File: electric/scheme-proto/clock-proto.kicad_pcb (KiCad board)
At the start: 2 copper layers, 60.5 x 88.5 mm, 134 parts, among them K1 servo, K2 1-wire, P1 batt, P10 led, P11 p2, P12 btn-4, P13 led, P14 led, P15 btn-5, P2 speaker, P3 dist, P4 btn-1, P5 btn-2, P6 btn-3, P7 led, P8 p1, P9 p3, Q1 bc857, Q10 bc847, Q11 bc847, Q12 bc857, Q13 bc857, Q14 bc847, Q15 bc847, Q16 bc847, Q17 bc857, Q18 bc857, Q2 bc847, Q3 bc857, Q4 bc847, Q5 irlml2244, Q6 bc847, Q7 bc857, Q8 bc847, Q9 bc857, U1 3310-LCD, U2 AD8607_2, U3 SD, U4 MINI-USB-B, U5 AD8607_2, U6 NCP3063, U7 NCP3063, U8 DS18S20

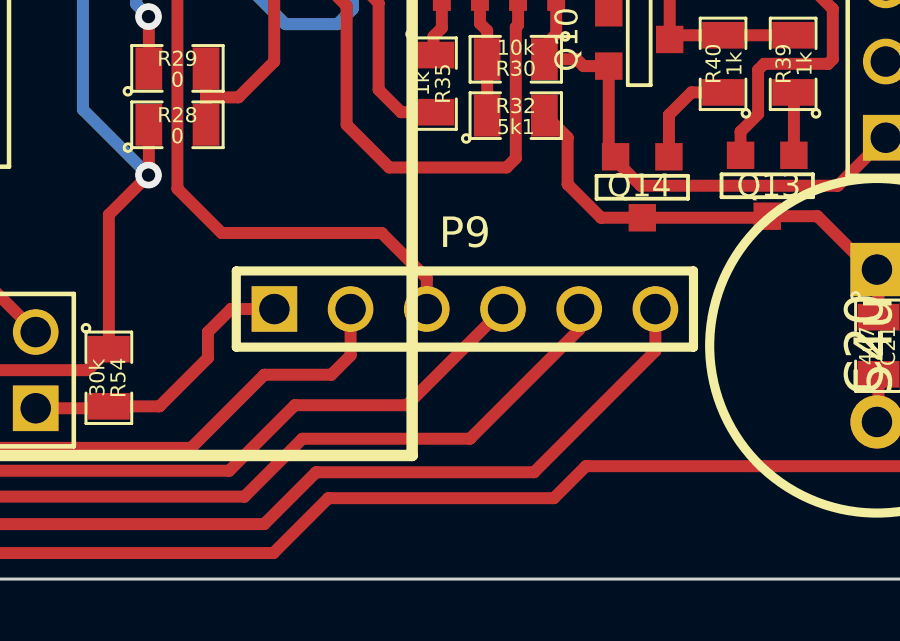
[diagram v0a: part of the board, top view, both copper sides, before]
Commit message: Shifted horizontal socket a bit upwards because, it didn't match the one on Disccovery board.
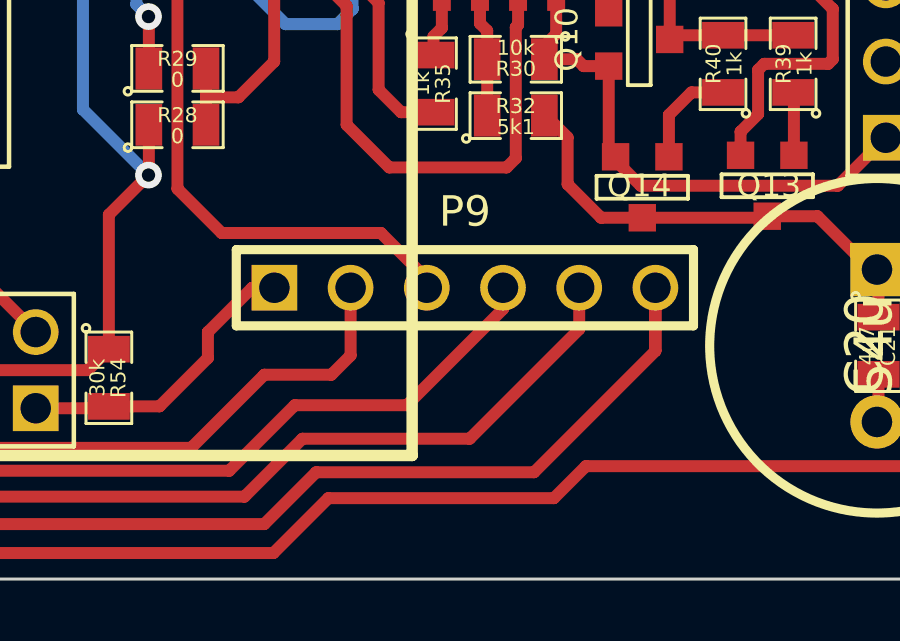
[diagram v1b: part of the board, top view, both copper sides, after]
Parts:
- moved P9 0.71 mm to (150.4, 139.3)
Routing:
- net /pb15: track 62.2 -> 65.0 mm
- net /pb12: track 35.6 -> 34.9 mm
- net /pb13: track 38.4 -> 39.1 mm
- net /btn-5: track 19.3 -> 20.0 mm
- net /pb14: track 37.4 -> 38.1 mm
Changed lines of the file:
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@@
     (area 119.449999 58.01106 180.050001 149.050001)
     (thickness 1.6)
-    (drawings 9)
-    (tracks 1178)
+    (drawings 10)
+    (tracks 1181)
     (zones 0)
     (modules 134)
@@
   )
   (setup
-    (last_trace_width 0.254)
+    (last_trace_width 0.4)
     (user_trace_width 0.4)
     (user_trace_width 0.6)
@@
   )
   (module PIN_ARRAY_6x1 (layer F.Cu)
-    (at 150.45 140)
+    (at 150.45 139.29)
     (descr "Double rangee de contacts 2 x 5 pins")
     (tags CONN)
@@
     )
   )
+  (gr_line (start 143.3 139.3) (end 157.4 139.3) (angle 90) (layer Dwgs.User) (width 0.2))
   (gr_line (start 119.5 149) (end 180 149) (angle 90) (layer Edge.Cuts) (width 0.1))
   (gr_line (start 124.5 60.5) (end 180 60.5) (angle 90) (layer Edge.Cuts) (width 0.1))
@@
   (segment (start 164.48 86.03) (end 164.6299 86.03) (width 0.4) (layer F.Cu) (net 12))
   (segment (start 164.6299 86.03) (end 168.5163 82.1436) (width 0.4) (layer F.Cu) (net 12))
+  (segment (start 141.8906 140.7606) (end 143.3612 139.29) (width 0.4) (layer F.Cu) (net 13) (status 800000))
+  (segment (start 143.3612 139.29) (end 144.1 139.29) (width 0.4) (layer F.Cu) (net 13) (status C00000))
   (segment (start 138.5824 143.2433) (end 140.2715 143.2433) (width 0.4) (layer F.Cu) (net 13))
-  (segment (start 142.6512 140) (end 144.1 140) (width 0.4) (layer F.Cu) (net 13))
-  (segment (start 141.8844 140.7668) (end 142.6512 140) (width 0.4) (layer F.Cu) (net 13))
+  (segment (start 141.8844 140.7668) (end 141.8906 140.7606) (width 0.4) (layer F.Cu) (net 13))
   (segment (start 141.8844 141.6304) (end 141.8844 140.7668) (width 0.4) (layer F.Cu) (net 13))
   (segment (start 140.2715 143.2433) (end 141.8844 141.6304) (width 0.4) (layer F.Cu) (net 13))
@@
   (segment (start 138.5189 143.3068) (end 138.5824 143.2433) (width 0.4) (layer F.Cu) (net 13))
   (segment (start 133.2484 143.3449) (end 133.3373 143.3449) (width 0.4) (layer F.Cu) (net 14))
-  (segment (start 146.64 141.5484) (end 146.64 140) (width 0.4) (layer F.Cu) (net 14))
+  (segment (start 146.64 141.5484) (end 146.64 139.29) (width 0.4) (layer F.Cu) (net 14) (status 20))
   (segment (start 145.9992 142.1892) (end 146.64 141.5484) (width 0.4) (layer F.Cu) (net 14))
   (segment (start 143.764 142.1892) (end 145.9992 142.1892) (width 0.4) (layer F.Cu) (net 14))
@@
   (segment (start 164.48 121.59) (end 161.6585 121.59) (width 0.4) (layer F.Cu) (net 29))
   (segment (start 161.6585 121.59) (end 161.544 121.4755) (width 0.4) (layer F.Cu) (net 29))
-  (segment (start 149.18 140) (end 149.18 138.9692) (width 0.4) (layer F.Cu) (net 30))
+  (segment (start 147.65 137.4648) (end 149.18 138.9948) (width 0.4) (layer F.Cu) (net 30) (status 800000))
+  (segment (start 149.18 138.9948) (end 149.18 139.29) (width 0.4) (layer F.Cu) (net 30) (status C00000))
   (segment (start 128.0668 124.5616) (end 124.5616 124.5616) (width 0.4) (layer F.Cu) (net 30))
   (segment (start 131.1148 127.6096) (end 128.0668 124.5616) (width 0.4) (layer F.Cu) (net 30))
@@
   (segment (start 140.8684 135.9916) (end 140.8684 129.1336) (width 0.4) (layer F.Cu) (net 30))
   (segment (start 142.3416 137.4648) (end 140.8684 135.9916) (width 0.4) (layer F.Cu) (net 30))
-  (segment (start 147.6756 137.4648) (end 142.3416 137.4648) (width 0.4) (layer F.Cu) (net 30))
-  (segment (start 149.18 138.9692) (end 147.6756 137.4648) (width 0.4) (layer F.Cu) (net 30))
+  (segment (start 147.65 137.4648) (end 142.3416 137.4648) (width 0.4) (layer F.Cu) (net 30))
+  (segment (start 148.5148 143.2052) (end 151.72 140) (width 0.4) (layer F.Cu) (net 31) (status 800000))
+  (segment (start 151.72 140) (end 151.72 139.29) (width 0.4) (layer F.Cu) (net 31) (status C00000))
   (segment (start 128.8288 144.1196) (end 128.778 144.1196) (width 0.4) (layer F.Cu) (net 31))
   (segment (start 128.0668 135.5852) (end 127.2032 134.7216) (width 0.4) (layer F.Cu) (net 31))
@@
   (segment (start 128.778 144.1196) (end 128.0668 143.4084) (width 0.4) (layer F.Cu) (net 31))
   (segment (start 127.2032 134.7216) (end 124.5616 134.7216) (width 0.4) (layer F.Cu) (net 31))
-  (segment (start 148.5148 143.2052) (end 151.72 140) (width 0.4) (layer F.Cu) (net 31))
   (segment (start 144.78 143.2052) (end 148.5148 143.2052) (width 0.4) (layer F.Cu) (net 31))
   (segment (start 142.5956 145.3896) (end 144.78 143.2052) (width 0.4) (layer F.Cu) (net 31))
@@
   (segment (start 129.7432 145.034) (end 133.7564 145.034) (width 0.4) (layer F.Cu) (net 31))
   (segment (start 128.8288 144.1196) (end 129.7432 145.034) (width 0.4) (layer F.Cu) (net 31))
+  (segment (start 150.61 144.3228) (end 154.26 140.6728) (width 0.4) (layer F.Cu) (net 32))
+  (segment (start 154.26 140.6728) (end 154.26 139.29) (width 0.4) (layer F.Cu) (net 32) (status 800000))
   (segment (start 124.5616 139.8016) (end 126.5936 139.8016) (width 0.4) (layer F.Cu) (net 32))
   (segment (start 127.254 144.018) (end 127.9652 144.7292) (width 0.4) (layer F.Cu) (net 32))
   (segment (start 127.254 140.462) (end 127.254 144.018) (width 0.4) (layer F.Cu) (net 32))
   (segment (start 126.5936 139.8016) (end 127.254 140.462) (width 0.4) (layer F.Cu) (net 32))
-  (segment (start 154.26 140) (end 154.26 140.6848) (width 0.4) (layer F.Cu) (net 32))
   (segment (start 129.4892 146.2532) (end 127.9652 144.7292) (width 0.4) (layer F.Cu) (net 32))
   (segment (start 143.1036 146.2532) (end 129.4892 146.2532) (width 0.4) (layer F.Cu) (net 32))
   (segment (start 145.034 144.3228) (end 143.1036 146.2532) (width 0.4) (layer F.Cu) (net 32))
-  (segment (start 150.622 144.3228) (end 145.034 144.3228) (width 0.4) (layer F.Cu) (net 32))
-  (segment (start 154.26 140.6848) (end 150.622 144.3228) (width 0.4) (layer F.Cu) (net 32))
+  (segment (start 150.61 144.3228) (end 145.034 144.3228) (width 0.4) (layer F.Cu) (net 32))
+  (segment (start 152.7556 145.4404) (end 156.8 141.396) (width 0.4) (layer F.Cu) (net 33))
+  (segment (start 156.8 141.396) (end 156.8 139.29) (width 0.4) (layer F.Cu) (net 33) (status 800000))
   (segment (start 128.6256 147.1676) (end 128.6256 147.1256) (width 0.4) (layer F.Cu) (net 33))
   (segment (start 121.2 127.8216) (end 121.92 127.1016) (width 0.4) (layer F.Cu) (net 33))
@@
   (segment (start 128.6256 147.1256) (end 124.9 143.4) (width 0.4) (layer F.Cu) (net 33))
   (segment (start 121.92 127.1016) (end 124.5616 127.1016) (width 0.4) (layer F.Cu) (net 33))
-  (segment (start 156.8 140) (end 156.8 141.396) (width 0.4) (layer F.Cu) (net 33))
+  (segment (start 156.8 139.29) (end 156.8 141.396) (width 0.4) (layer F.Cu) (net 33) (status 10))
   (segment (start 121.92 127.1016) (end 124.5616 127.1016) (width 0.4) (layer F.Cu) (net 33))
   (segment (start 143.764 147.1676) (end 128.6256 147.1676) (width 0.4) (layer F.Cu) (net 33))
   (segment (start 145.4912 145.4404) (end 143.764 147.1676) (width 0.4) (layer F.Cu) (net 33))
   (segment (start 152.7556 145.4404) (end 145.4912 145.4404) (width 0.4) (layer F.Cu) (net 33))
-  (segment (start 156.8 141.396) (end 152.7556 145.4404) (width 0.4) (layer F.Cu) (net 33))
   (segment (start 164.48 75.87) (end 165.0744 75.87) (width 0.4) (layer F.Cu) (net 34))
   (segment (start 167.386 67.6148) (end 167.9067 67.6148) (width 0.4) (layer F.Cu) (net 34))

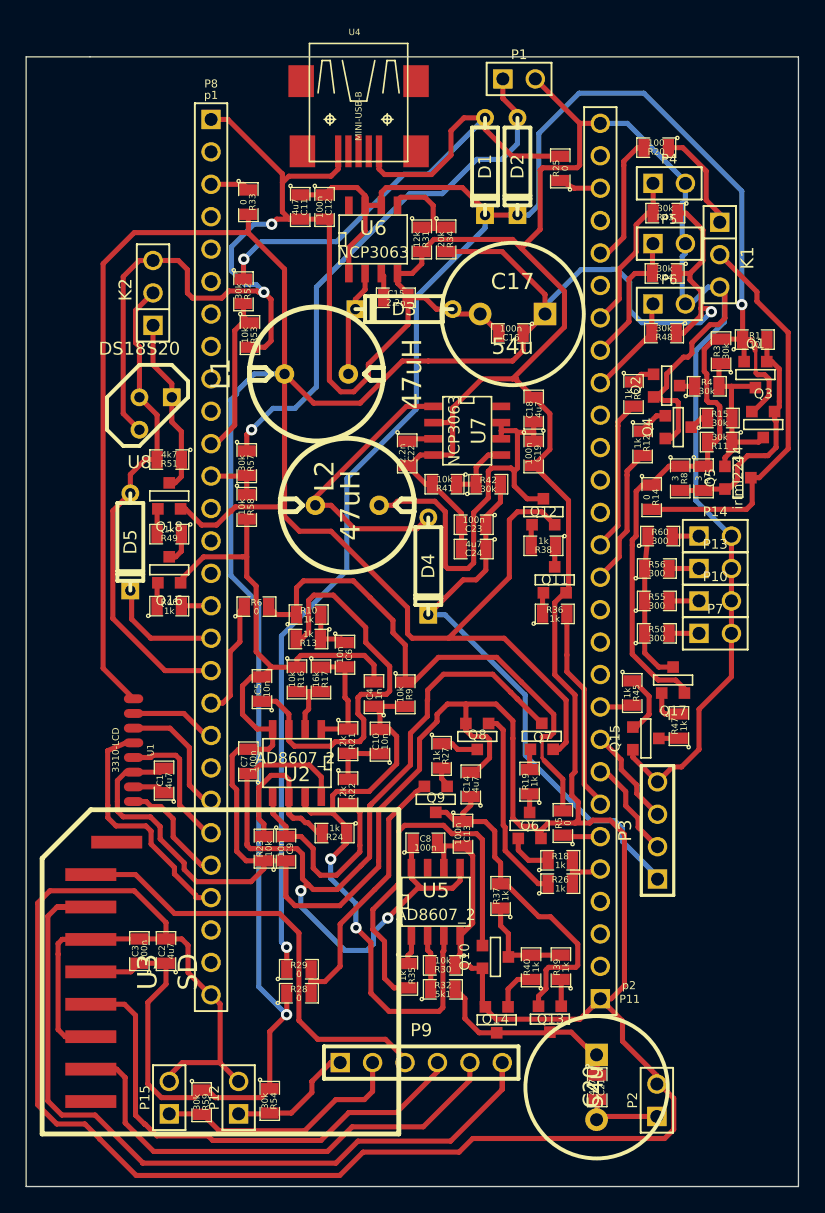
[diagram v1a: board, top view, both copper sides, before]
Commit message: Radically simplified audio scheme.
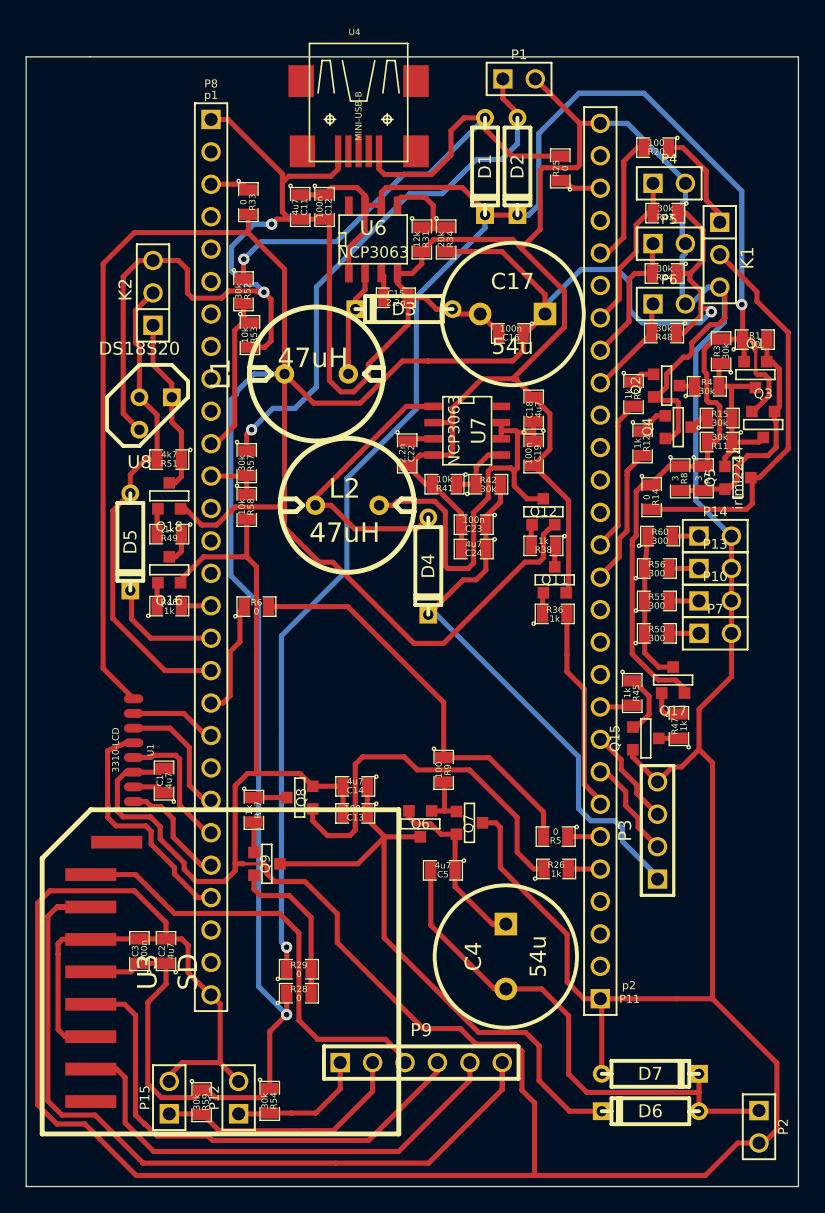
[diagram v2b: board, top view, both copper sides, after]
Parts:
- removed C10, C6, C9: 10n, SM0805
- removed C20: 54u, C2V10
- removed C21: 4u7, SM0805
- removed C7, C8: 100n, SM0805
- removed Q10, Q14: bc847, SOT23EBC
- removed Q13: bc857, SOT23EBC
- removed R10, R13, R18, R19, R24, R35, R37, R39, R40: 1k, SM0805
- removed R16, R23, R30: 10k, SM0805
- removed R17: 16k, SM0805
- removed R21, R22: 2k, SM0805
- removed R32: 5k1, SM0805
- removed U2, U5: AD8607_2, SO8E
- added D6: 1N5819, D3, F.Cu at (168.4, 143.1)
- added D7: 1N5819, D3, F.Cu at (168.4, 140.2)
- C4: value 1n -> 54u; footprint SM0805 -> C2V10
- C5: value 10n -> 4u7
- R9: value 10k -> 100
- moved C4 23.0 mm to (157.1, 131.0), turned to 270 degrees
- moved C5 20.1 mm to (152.2, 124.2), turned to 180 degrees
- moved R27 15.3 mm to (137.3, 119.5)
- moved Q8 14.7 mm to (140.9, 118.5), turned to 270 degrees
- moved Q9 14.2 mm to (138.4, 123.7), turned to 90 degrees
- moved C14 9.05 mm to (145.3, 117.7), turned to 180 degrees
- moved Q7 8.84 mm to (154.2, 120.5), turned to 90 degrees
- moved C13 8.59 mm to (145.3, 119.8), turned to 180 degrees
- moved Q6 8.56 mm to (150.4, 120.6), turned to 0 degrees
- moved P2 8.27 mm to (176.9, 144.3), turned to 270 degrees
- moved R9 6.64 mm to (152.2, 116.4)
- moved R5 1.21 mm to (161.0, 121.6), turned to 180 degrees
- moved R26 1.20 mm to (161.0, 124.1)
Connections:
- C13 pad 1: N-0000092 (its old number) -> N-0000072
- C14 pad 1: N-0000092 (its old number) -> N-0000072
- C4 pad 1: /snd-amp-in -> N-0000055
- C4 pad 2: GND -> /speaker-1
- C5 pad 1: N-00000107 -> N-0000055
- C5 pad 2: GND -> /speaker-1
- Q6 pad 1: GND -> N-0000055
- Q6 pad 2: N-00000117 -> N-0000051
- Q6 pad 3: N-00000118 -> N-0000072
- Q7 pad 1: VDD -> N-0000055
- Q7 pad 2: N-00000119 -> N-0000051
- Q7 pad 3: /filter-vdd -> GND
- Q9 pad 3: N-0000092 (its old number) -> N-0000072
- R9 pad 2: /snd-amp-in -> N-0000051
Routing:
- net /filter-vdd: track 76.5 -> 0.00 mm, vias 2 -> 0
- net N-0000072: track 0.00 -> 48.5 mm
- net /snd-amp-in: track 47.1 -> 0.00 mm, vias 2 -> 0
- net /speaker-1: track 6.44 -> 41.1 mm
- net GND: track 606.1 -> 573.9 mm
- net N-00000107: track 32.1 -> 0.00 mm
- net N-0000023: track 30.5 -> 0.00 mm
- net N-0000092 (its old number): track 27.2 -> 0.00 mm
- net VDD: track 289.5 -> 271.0 mm
- net N-00000111: track 16.6 -> 0.00 mm
- net N-0000093 (its old number): track 15.8 -> 0.00 mm
- net N-0000063: track 15.3 -> 30.3 mm
- net N-0000055: track 0.00 -> 14.1 mm
- net N-00000113: track 13.3 -> 0.00 mm
- net N-0000080: track 42.1 -> 32.7 mm
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
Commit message: Remade amplifier scheme and rerouted the whole scheme respectively.
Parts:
- removed D6, D7: 1N5819, D3
- added C6: 4n, SM0805, F.Cu at (151.4, 111.3)
- added C7: 1n, SM0805, F.Cu at (153.4, 116.8)
- added C8: 68n, SM0805, F.Cu at (145.3, 119.4)
- added C9: 1n, SM0805, F.Cu at (149.3, 127.3)
- added Q10: bc857, SOT23EBC, F.Cu at (152.4, 128.3)
- added Q13: bc847, SOT23EBC, F.Cu at (155.4, 132.3)
- added R10: 10k, SM0805, F.Cu at (151.4, 113.3)
- added R13: 20k, SM0805, F.Cu at (155.4, 116.8)
- added R16: 2k7, SM0805, F.Cu at (144.9, 124.3)
- added R17: 1k3, SM0805, F.Cu at (147.9, 124.3)
- added R18: 2k7, SM0805, F.Cu at (146.8, 127.3)
- added R19: 15k, SM0805, F.Cu at (140.7, 121.0)
- added R21: 1k8, SM0805, F.Cu at (140.7, 117.5)
- added R22: 10k, SM0805, F.Cu at (140.7, 114.0)
- added R23: 3k, SM0805, F.Cu at (153.4, 124.3)
- added R24: 3k, SM0805, F.Cu at (155.4, 124.3)
- added U2: AD8607_2, SO8E, F.Cu at (149.4, 119.3)
- C4: value 54u -> 47u
- R9: value 100 -> 20k
- moved C5 27.7 mm to (173.1, 142.4), turned to 270 degrees
- moved C4 19.7 mm to (173.1, 142.4)
- moved Q7 12.2 mm to (150.9, 132.3), turned to 270 degrees
- moved Q6 10.1 mm to (156.9, 128.3), turned to 90 degrees
- moved C14 9.92 mm to (137.5, 111.5), turned to 270 degrees
- moved C13 8.23 mm to (153.4, 120.8), turned to 90 degrees
- moved R9 4.46 mm to (155.4, 113.3)
- moved Q8 4.21 mm to (138.0, 115.5), turned to 0 degrees
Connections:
- C13 pad 1: N-0000072 (its old number) -> /opamp-vcc
- C14 pad 1: N-0000072 (its old number) -> /opamp-vcc
- Q6 pad 2: N-0000051 (its old number) -> N-0000043
- Q6 pad 3: N-0000072 (its old number) -> /opamp-vcc
- Q7 pad 2: N-0000051 (its old number) -> N-0000042
- Q9 pad 3: N-0000072 (its old number) -> /opamp-vcc
- R9 pad 2: N-0000051 (its old number) -> N-0000037
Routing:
- net /opamp-vcc: track 0.00 -> 63.6 mm
- net N-0000072 (its old number): track 48.5 -> 0.00 mm
- net /speaker-1: track 41.1 -> 6.20 mm
- net N-0000056: track 14.1 -> 38.4 mm, vias 0 -> 2
- net GND: track 573.9 -> 596.1 mm
- net /ref_5v: track 0.00 -> 21.1 mm
- net N-0000042: track 0.00 -> 17.6 mm
- net N-0000032: track 0.00 -> 15.6 mm
- net /ref_3v3: track 0.00 -> 13.0 mm
- net N-0000038: track 0.00 -> 11.2 mm
- net N-0000034: track 0.00 -> 10.8 mm
- net N-0000037: track 0.00 -> 7.04 mm
- net N-0000031: track 0.00 -> 6.96 mm
- net N-0000043: track 0.00 -> 4.63 mm
- net N-0000041: track 0.00 -> 4.48 mm
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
